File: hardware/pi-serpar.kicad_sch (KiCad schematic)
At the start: 31 parts, among them J2 40HAT, J3 IEEE1284, J4 IEEE1284, J5 RS232, J7 RS232, U1 CAT24C32, U2 SN74LVC161284DLR, U3 MAX3232

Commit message: v1 ordered at jlcpcb
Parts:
- JP1: footprint Jumper:SolderJumper-2_P1.3mm_Open_RoundedPad1.0x1.5mm -> Jumper:SolderJumper-2_P1.3mm_Bridged_Pad1.0x1.5mm; symbol Jumper:SolderJumper_2_Open -> Jumper:SolderJumper_2_Bridged
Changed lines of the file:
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@@
     )
   )
-  (symbol (lib_id "Jumper:SolderJumper_2_Open") (at 40.64 190.5 0) (unit 1)
+  (symbol (lib_id "Jumper:SolderJumper_2_Bridged") (at 40.64 190.5 0) (unit 1)
     (in_bom yes) (on_board yes) (dnp no) (fields_autoplaced)
-    (property "Reference" "JP1" (at 40.64 184.404 0)
+    (property "Reference" "JP1" (at 40.64 184.15 0)
       (effects (font (size 1.27 1.27)))
     )
-    (property "Value" "EEPROM WP" (at 40.64 186.944 0)
+    (property "Value" "EEPROM WP" (at 40.64 186.69 0)
       (effects (font (size 1.27 1.27)))
     )
-    (property "Footprint" "Jumper:SolderJumper-2_P1.3mm_Open_RoundedPad1.0x1.5mm" (at 40.64 190.5 0)
+    (property "Footprint" "Jumper:SolderJumper-2_P1.3mm_Bridged_Pad1.0x1.5mm" (at 40.64 190.5 0)
       (effects (font (size 1.27 1.27)) hide)
     )

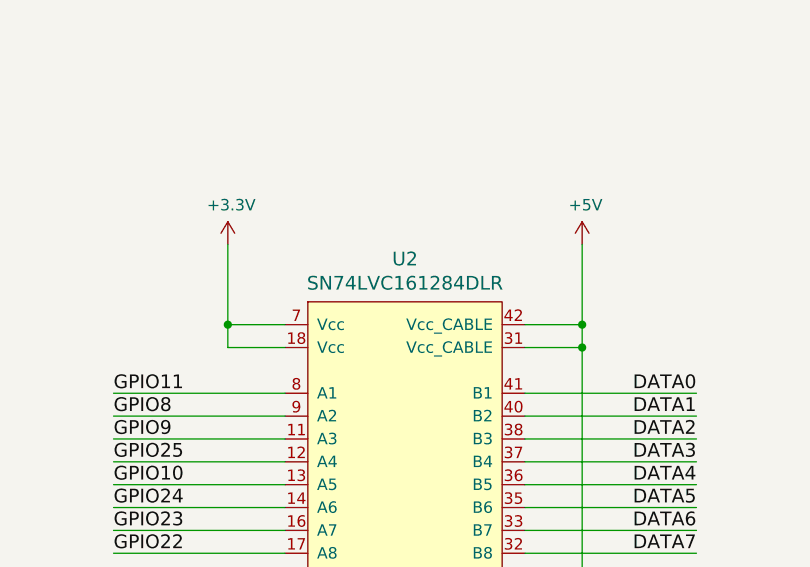
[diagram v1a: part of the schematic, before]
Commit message: IEEE1284 in TSSOP-48 package
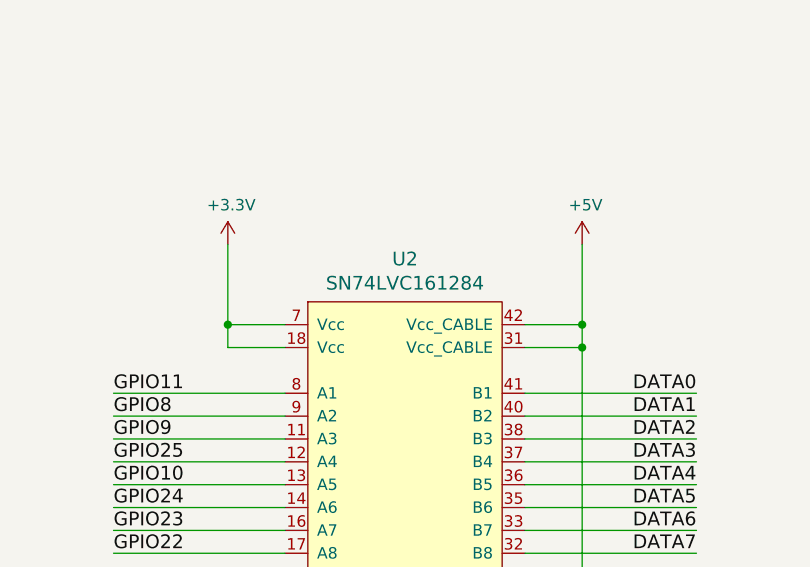
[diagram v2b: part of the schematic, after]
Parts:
- U2: value SN74LVC161284DLR -> SN74LVC161284; footprint Package_SO:SSOP-48_7.5x15.9mm_P0.635mm -> Package_SO:TSSOP-48_6.1x12.5mm_P0.5mm
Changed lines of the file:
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@@
       (effects (font (size 1.524 1.524)))
     )
-    (property "Value" "SN74LVC161284DLR" (at 182.245 166.8526 0)
+    (property "Value" "SN74LVC161284" (at 182.245 166.8526 0)
       (effects (font (size 1.524 1.524)))
     )
-    (property "Footprint" "Package_SO:SSOP-48_7.5x15.9mm_P0.635mm" (at 200.66 184.15 0)
+    (property "Footprint" "Package_SO:TSSOP-48_6.1x12.5mm_P0.5mm" (at 200.66 184.15 0)
       (effects (font (size 1.524 1.524)) hide)
     )

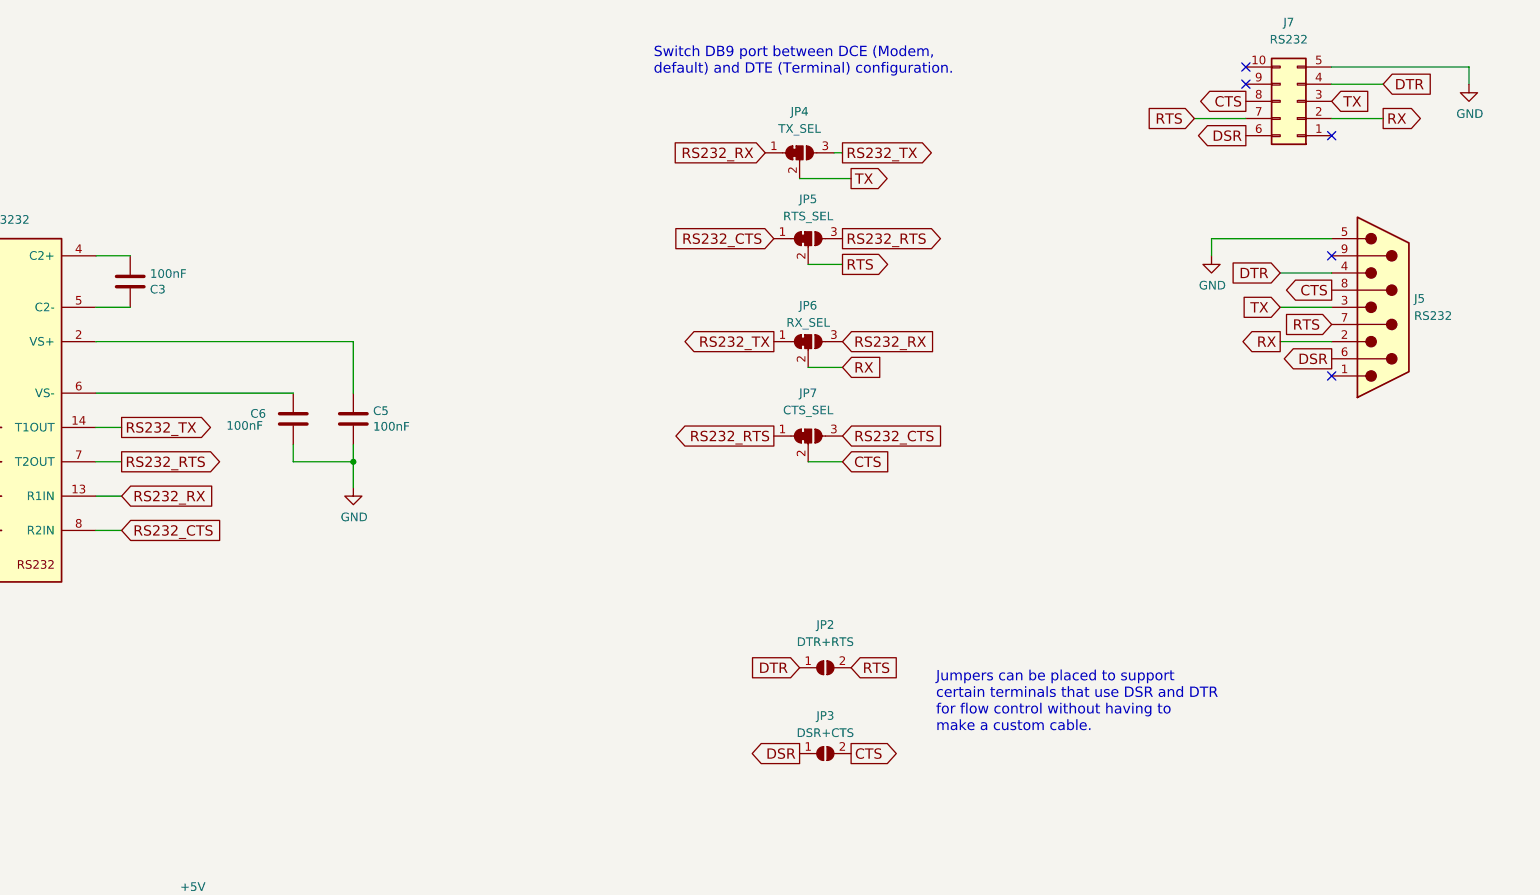
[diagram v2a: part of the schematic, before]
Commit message: fix idc footprints, add db9h
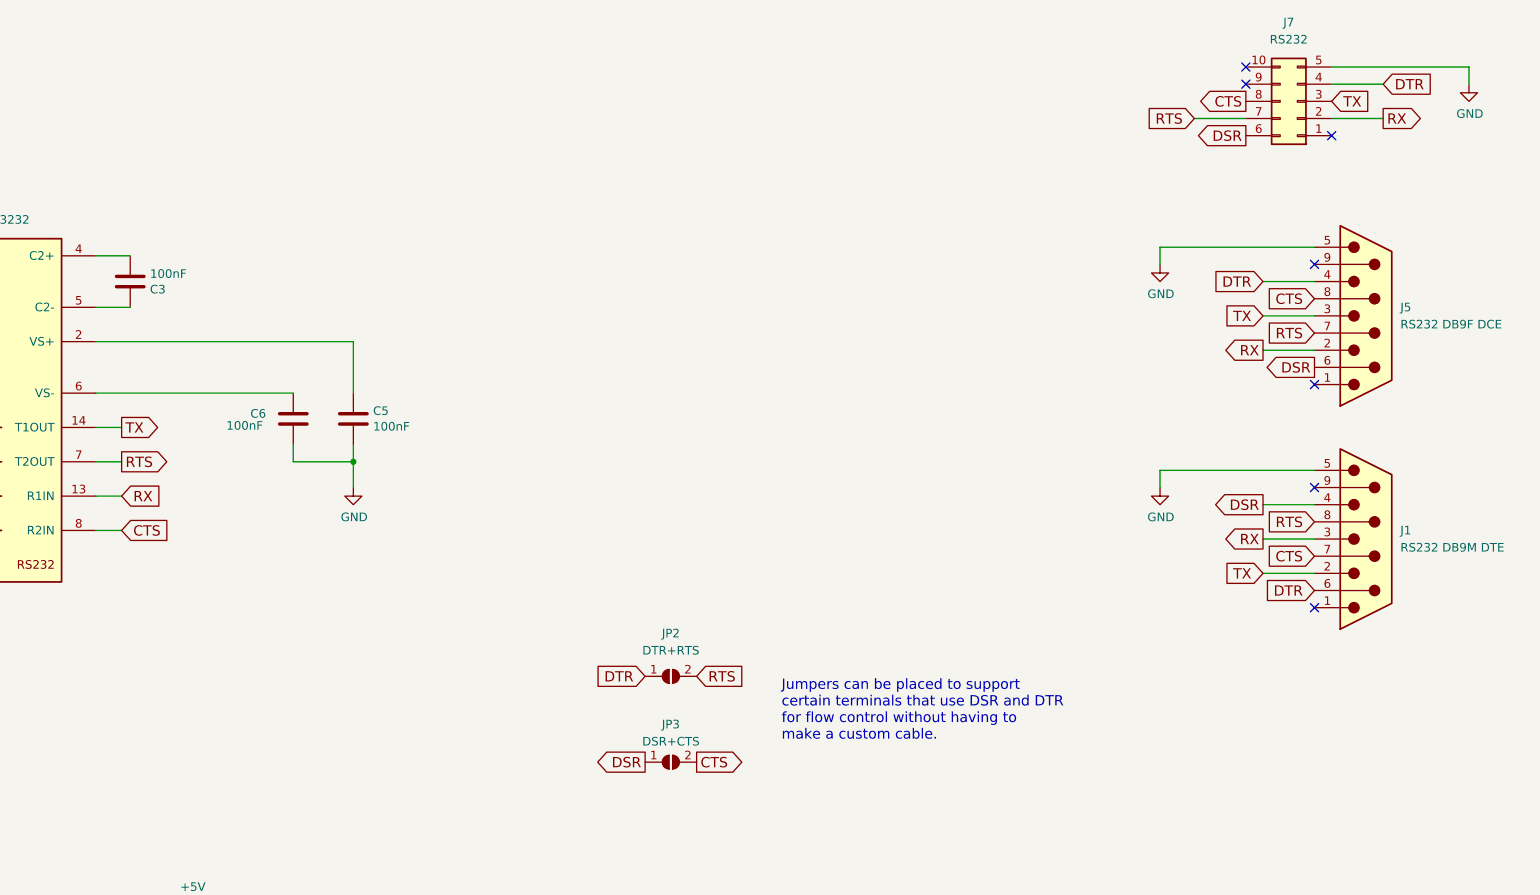
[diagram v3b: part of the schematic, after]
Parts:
- removed JP4: TX_SEL, Jumper:SolderJumper-3_P1.3mm_Bridged12_RoundedPad1.0x1.5mm, symbol Jumper:SolderJumper_3_Bridged12
- removed JP5: RTS_SEL, Jumper:SolderJumper-3_P1.3mm_Bridged12_RoundedPad1.0x1.5mm, symbol Jumper:SolderJumper_3_Bridged12
- removed JP6: RX_SEL, Jumper:SolderJumper-3_P1.3mm_Bridged12_RoundedPad1.0x1.5mm, symbol Jumper:SolderJumper_3_Bridged12
- removed JP7: CTS_SEL, Jumper:SolderJumper-3_P1.3mm_Bridged12_RoundedPad1.0x1.5mm, symbol Jumper:SolderJumper_3_Bridged12
- added J1: RS232 DB9M DTE, Connector_Dsub:DSUB-9_Male_Horizontal_P2.77x2.84mm_EdgePinOffset7.70mm_Housed_MountingHolesOffset9.12mm, symbol Connector:DE9_Plug
- J5: value RS232 -> RS232 DB9F DCE; footprint Connector_Dsub:DSUB-9_Male_Horizontal_P2.77x2.84mm_EdgePinOffset7.70mm_Housed_MountingHolesOffset9.12mm -> Connector_Dsub:DSUB-9_Female_Horizontal_P2.77x2.84mm_EdgePinOffset7.70mm_Housed_MountingHolesOffset9.12mm
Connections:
- net RS232_CTS is gone; now on net CTS: U3.8 (R2IN)
- net RS232_RTS is gone; now on net RTS: U3.7 (T2OUT)
- net RS232_RX is gone; now on net RX: U3.13 (R1IN)
- net RS232_TX is gone; now on net TX: U3.14 (T1OUT)
- net CTS: now also J1.7
- net DSR: now also J1.4
- net DTR: now also J1.6
- net GND: now also J1.5
- net RTS: now also J1.8
- net RX: now also J1.3
- net TX: now also J1.2
- no-connect marks 11 -> 13
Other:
- note removed: "Switch DB9 port between DCE (Modem, default) and DTE (Terminal) configuration."
- moved on the sheet: J5, JP2, JP3

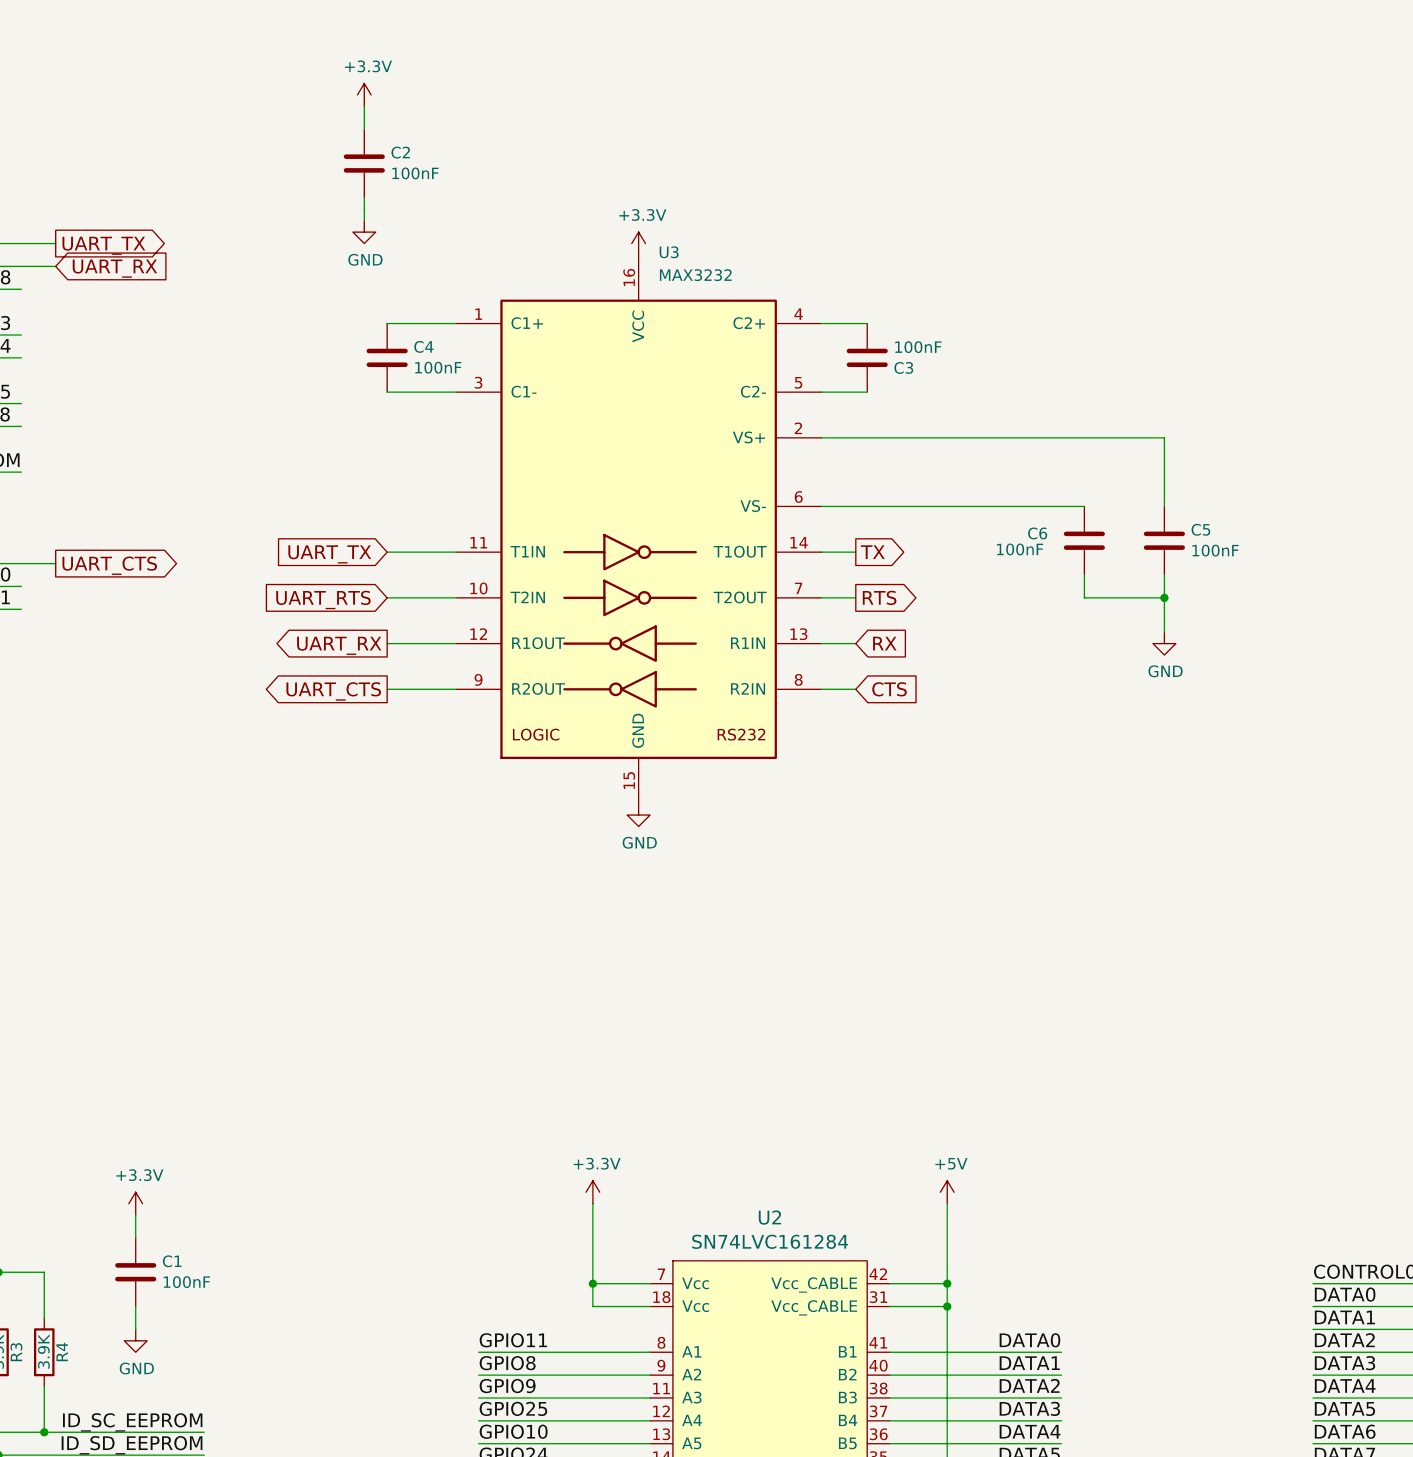
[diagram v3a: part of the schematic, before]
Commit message: v3 with dual db9 footprints
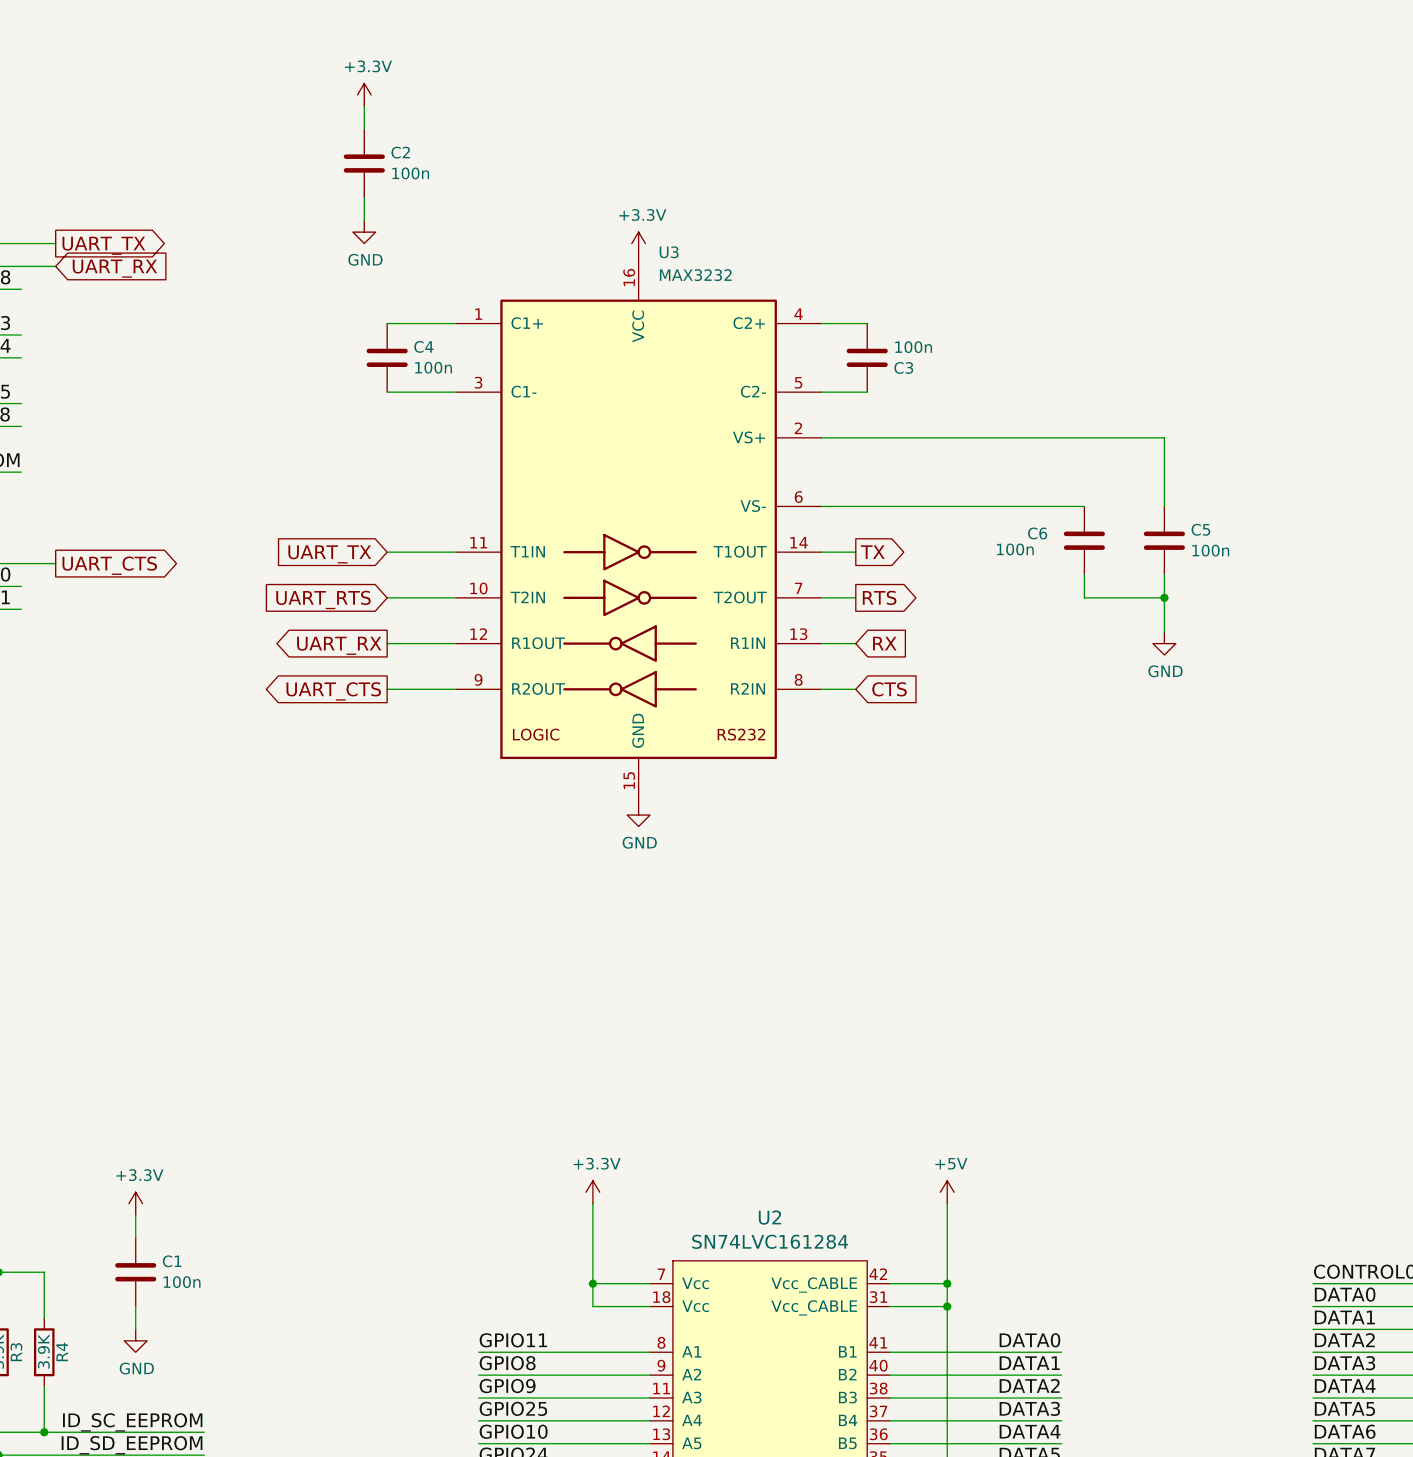
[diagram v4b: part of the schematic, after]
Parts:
- C1, C2, C3, C4, C5, C6: value 100nF -> 100n
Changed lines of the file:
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@@
       (effects (font (size 1.27 1.27)) (justify left))
     )
-    (property "Value" "100nF" (at 140.081 48.133 0)
+    (property "Value" "100n" (at 140.081 48.133 0)
       (effects (font (size 1.27 1.27)) (justify left))
     )
@@
       (effects (font (size 1.27 1.27)) (justify left))
     )
-    (property "Value" "100nF" (at 114.681 171.323 0)
+    (property "Value" "100n" (at 114.681 171.323 0)
       (effects (font (size 1.27 1.27)) (justify left))
     )
@@
       (effects (font (size 1.27 1.27)) (justify left))
     )
-    (property "Value" "100nF" (at 142.621 69.723 0)
+    (property "Value" "100n" (at 142.621 69.723 0)
       (effects (font (size 1.27 1.27)) (justify left))
     )
@@
       (effects (font (size 1.27 1.27)) (justify left))
     )
-    (property "Value" "100nF" (at 207.264 89.916 0)
+    (property "Value" "100n" (at 207.264 89.916 0)
       (effects (font (size 1.27 1.27)) (justify left))
     )
@@
       (effects (font (size 1.27 1.27)) (justify left))
     )
-    (property "Value" "100nF" (at 195.961 67.437 0)
+    (property "Value" "100n" (at 195.961 67.437 0)
       (effects (font (size 1.27 1.27)) (justify left))
     )
@@
       (effects (font (size 1.27 1.27)) (justify left))
     )
-    (property "Value" "100nF" (at 228.981 90.043 0)
-      (effects (font (size 1.27 1.27)) (justify left))
-    )
+    (property "Value" "100n" (at 228.981 90.043 0)
+      (effects (font (size 1.27 1.27)) (justify left))
+    )
